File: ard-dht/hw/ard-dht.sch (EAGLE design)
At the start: 7 parts, among them U1 ATMEGA328P_PDIP

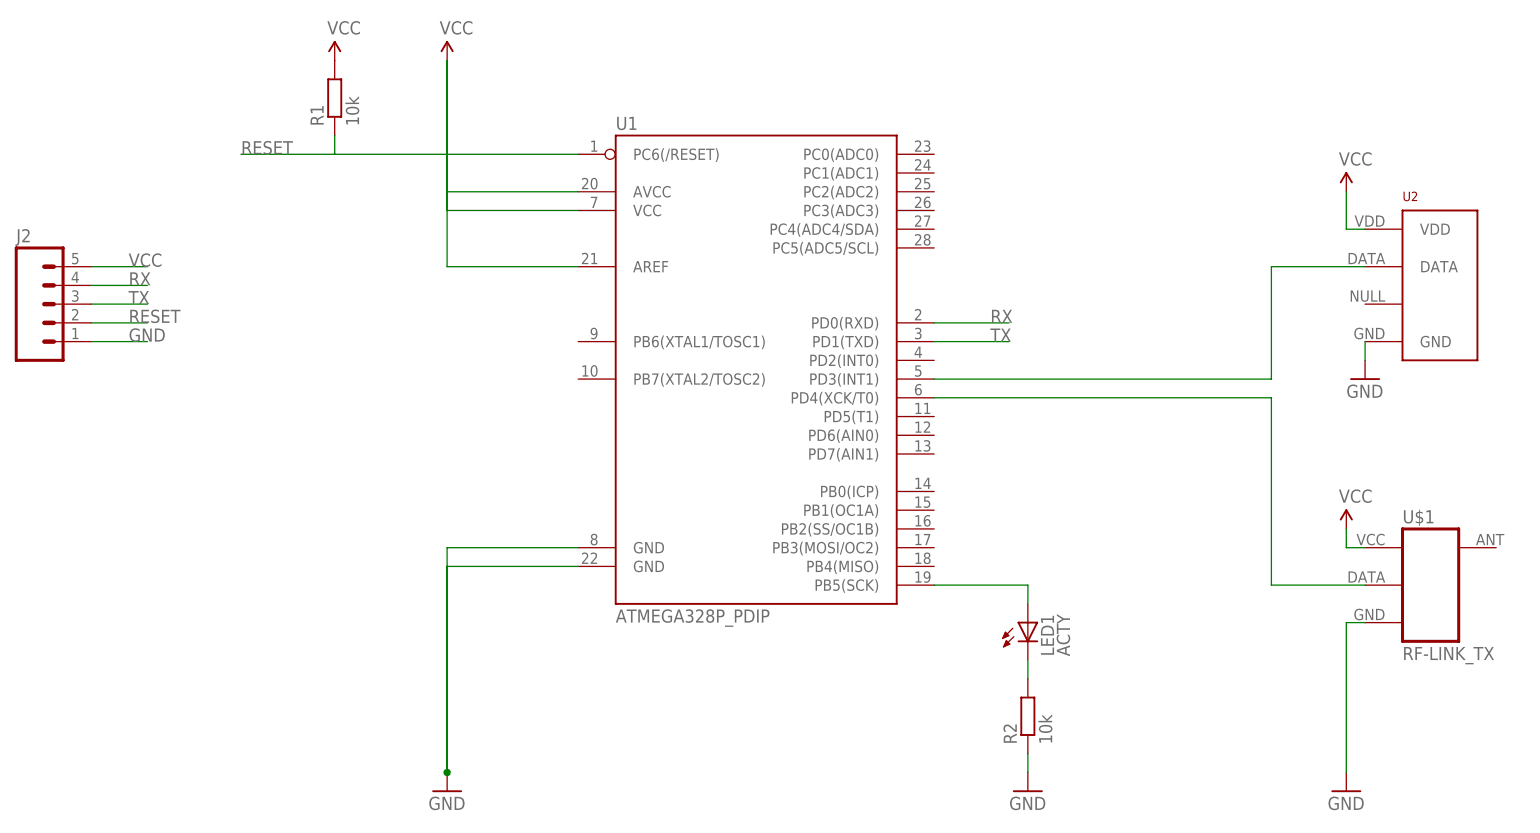
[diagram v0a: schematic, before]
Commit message: Using I/O pins to provide power to : 	- Temperature sensor (DHT) 	- RF emitter The Atmega328p is now used fully in power down mode. Wake up is performed regularly by using an external RC pair. Moved also the led output pin, the ease routing.
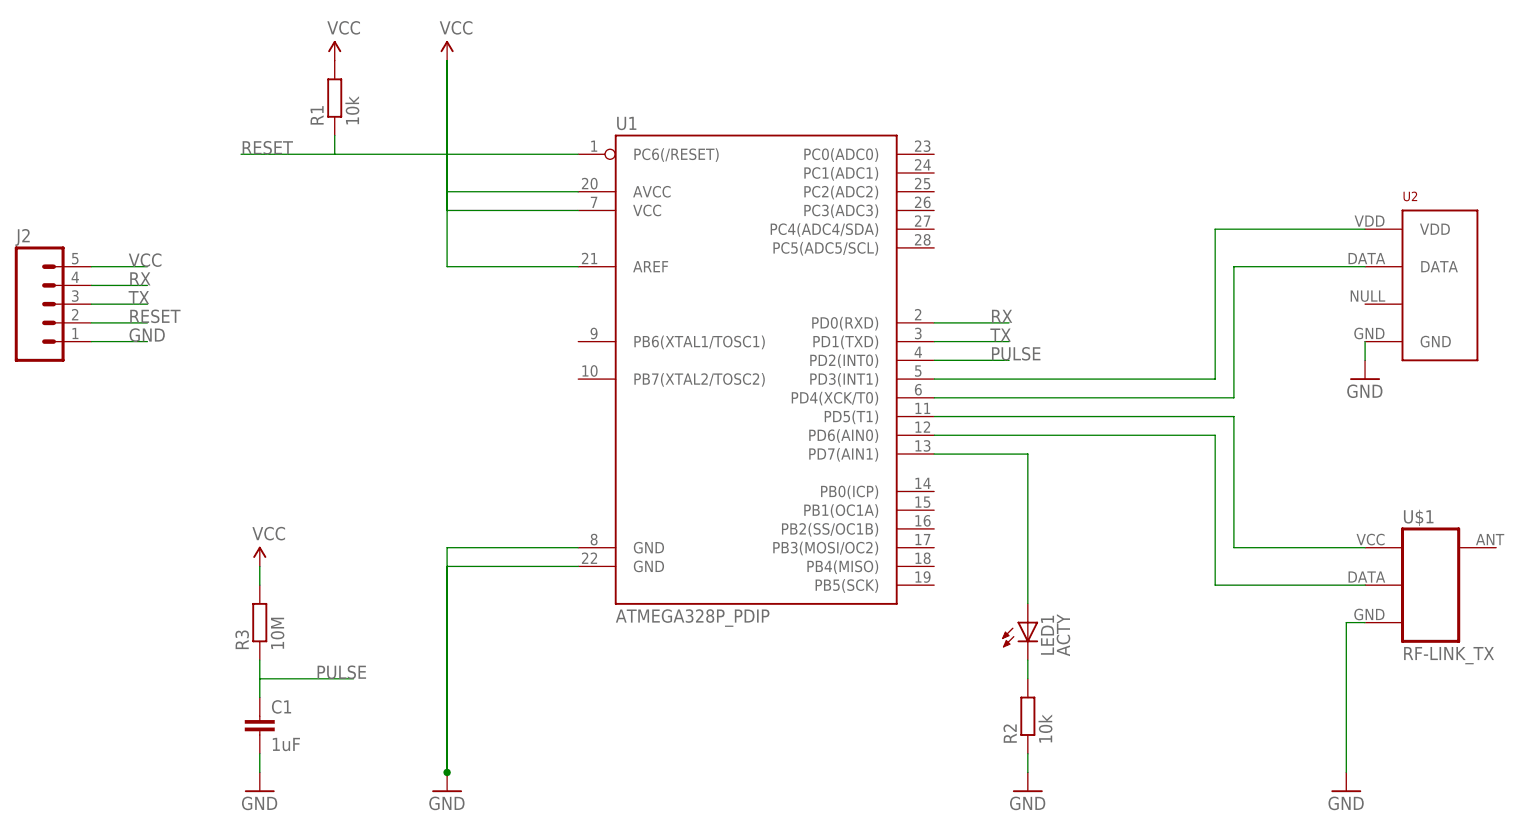
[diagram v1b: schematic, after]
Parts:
- added C1: 1uF, capacitor-wima:C5/5
- added R3: 10M, eagle-ltspice:R0204/7
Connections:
- new net N$5: U1.PD4(XCK/T0), U2.DATA
- new net N$6: U$1.DATA, U1.PD6(AIN0)
- new net PULSE: C1.1, R3.1, U1.PD2(INT0)
- net GND: now also C1.2
- net N$1: now also U2.VDD; no longer U2.DATA
- net N$2: now also U$1.+5V, U1.PD5(T1); no longer U$1.DATA, U1.PD4(XCK/T0)
- net N$3: now also U1.PD7(AIN1); no longer U1.PB5(SCK)
- net VCC: now also R3.2; no longer U$1.+5V, U2.VDD
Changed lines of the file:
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@@
 <part name="R1" library="resistor" deviceset="R-EU_" device="0207/10" value="10k"/>
 <part name="U2" library="RHT03_DHT-22_AM2302" deviceset="RHT03_DHT-22_AM2302" device=""/>
-<part name="SUPPLY3" library="SparkFun-Aesthetics" deviceset="VCC" device=""/>
 <part name="GND2" library="SparkFun-Aesthetics" deviceset="GND" device=""/>
 <part name="U$1" library="SparkFun-RF" deviceset="RF-LINK_TX" device=""/>
-<part name="SUPPLY4" library="SparkFun-Aesthetics" deviceset="VCC" device=""/>
 <part name="GND4" library="SparkFun-Aesthetics" deviceset="GND" device=""/>
 <part name="GND6" library="SparkFun-Aesthetics" deviceset="GND" device=""/>
@@
 <part name="LED1" library="led" deviceset="LED" device="3MM" value="ACTY"/>
 <part name="R2" library="eagle-ltspice" deviceset="R" device="0204/7" value="10k"/>
+<part name="GND3" library="SparkFun-Aesthetics" deviceset="GND" device=""/>
+<part name="SUPPLY3" library="SparkFun-Aesthetics" deviceset="VCC" device=""/>
+<part name="C1" library="capacitor-wima" deviceset="C" device="5/5" value="1uF"/>
+<part name="R3" library="eagle-ltspice" deviceset="R" device="0204/7" value="10M"/>
 </parts>
 <sheets>
@@
 <instance part="R1" gate="G$1" x="17.78" y="86.36" rot="R90"/>
 <instance part="U2" gate="G$1" x="167.64" y="60.96"/>
-<instance part="SUPPLY3" gate="G$1" x="154.94" y="73.66"/>
 <instance part="GND2" gate="1" x="157.48" y="48.26"/>
 <instance part="U$1" gate="G$1" x="165.1" y="22.86"/>
-<instance part="SUPPLY4" gate="G$1" x="154.94" y="27.94"/>
 <instance part="GND4" gate="1" x="154.94" y="-7.62"/>
 <instance part="GND6" gate="1" x="111.76" y="-7.62"/>
@@
 <instance part="LED1" gate="G$1" x="111.76" y="15.24"/>
 <instance part="R2" gate="G$1" x="111.76" y="2.54" rot="R90"/>
+<instance part="GND3" gate="1" x="7.62" y="-7.62"/>
+<instance part="SUPPLY3" gate="G$1" x="7.62" y="22.86"/>
+<instance part="C1" gate="G$1" x="7.62" y="2.54"/>
+<instance part="R3" gate="G$1" x="7.62" y="15.24" rot="R90"/>
 </instances>
 <busses>
@@
 </segment>
 <segment>
-<pinref part="U2" gate="G$1" pin="VDD"/>
-<wire x1="157.48" y1="68.58" x2="154.94" y2="68.58" width="0.1524" layer="91"/>
-<pinref part="SUPPLY3" gate="G$1" pin="VCC"/>
-<wire x1="154.94" y1="68.58" x2="154.94" y2="73.66" width="0.1524" layer="91"/>
-</segment>
-<segment>
-<pinref part="U$1" gate="G$1" pin="+5V"/>
-<wire x1="157.48" y1="25.4" x2="154.94" y2="25.4" width="0.1524" layer="91"/>
-<pinref part="SUPPLY4" gate="G$1" pin="VCC"/>
-<wire x1="154.94" y1="25.4" x2="154.94" y2="27.94" width="0.1524" layer="91"/>
-</segment>
-<segment>
 <pinref part="J2" gate="G$1" pin="5"/>
 <wire x1="-15.24" y1="63.5" x2="-7.62" y2="63.5" width="0.1524" layer="91"/>
 <label x="-10.16" y="63.5" size="1.778" layer="95"/>
+</segment>
+<segment>
+<pinref part="SUPPLY3" gate="G$1" pin="VCC"/>
+<pinref part="R3" gate="G$1" pin="2"/>
+<wire x1="7.62" y1="22.86" x2="7.62" y2="20.32" width="0.1524" layer="91"/>
 </segment>
 </net>
@@
 <wire x1="111.76" y1="-2.54" x2="111.76" y2="-5.08" width="0.1524" layer="91"/>
 </segment>
-</net>
-<net name="N$1" class="0">
-<segment>
-<pinref part="U1" gate="G$1" pin="PD3(INT1)"/>
-<wire x1="99.06" y1="48.26" x2="144.78" y2="48.26" width="0.1524" layer="91"/>
-<pinref part="U2" gate="G$1" pin="DATA"/>
-<wire x1="157.48" y1="63.5" x2="144.78" y2="63.5" width="0.1524" layer="91"/>
-<wire x1="144.78" y1="63.5" x2="144.78" y2="48.26" width="0.1524" layer="91"/>
-</segment>
-</net>
-<net name="N$2" class="0">
-<segment>
-<pinref part="U1" gate="G$1" pin="PD4(XCK/T0)"/>
-<wire x1="99.06" y1="45.72" x2="144.78" y2="45.72" width="0.1524" layer="91"/>
-<wire x1="144.78" y1="45.72" x2="144.78" y2="20.32" width="0.1524" layer="91"/>
-<pinref part="U$1" gate="G$1" pin="DATA"/>
-<wire x1="144.78" y1="20.32" x2="157.48" y2="20.32" width="0.1524" layer="91"/>
+<segment>
+<pinref part="C1" gate="G$1" pin="2"/>
+<pinref part="GND3" gate="1" pin="GND"/>
+<wire x1="7.62" y1="-2.54" x2="7.62" y2="-5.08" width="0.1524" layer="91"/>
 </segment>
 </net>
@@
 </segment>
 </net>
-<net name="N$3" class="0">
-<segment>
-<pinref part="U1" gate="G$1" pin="PB5(SCK)"/>
-<wire x1="99.06" y1="20.32" x2="111.76" y2="20.32" width="0.1524" layer="91"/>
-<pinref part="LED1" gate="G$1" pin="A"/>
-<wire x1="111.76" y1="20.32" x2="111.76" y2="17.78" width="0.1524" layer="91"/>
-</segment>
-</net>
 <net name="N$4" class="0">
 <segment>
@@
 </segment>
 </net>
+<net name="N$3" class="0">
+<segment>
+<pinref part="U1" gate="G$1" pin="PD7(AIN1)"/>
+<wire x1="99.06" y1="38.1" x2="111.76" y2="38.1" width="0.1524" layer="91"/>
+<pinref part="LED1" gate="G$1" pin="A"/>
+<wire x1="111.76" y1="38.1" x2="111.76" y2="17.78" width="0.1524" layer="91"/>
+</segment>
+</net>
+<net name="N$1" class="0">
+<segment>
+<pinref part="U1" gate="G$1" pin="PD3(INT1)"/>
+<wire x1="99.06" y1="48.26" x2="137.16" y2="48.26" width="0.1524" layer="91"/>
+<wire x1="137.16" y1="48.26" x2="137.16" y2="68.58" width="0.1524" layer="91"/>
+<pinref part="U2" gate="G$1" pin="VDD"/>
+<wire x1="137.16" y1="68.58" x2="157.48" y2="68.58" width="0.1524" layer="91"/>
+</segment>
+</net>
+<net name="N$5" class="0">
+<segment>
+<pinref part="U1" gate="G$1" pin="PD4(XCK/T0)"/>
+<wire x1="99.06" y1="45.72" x2="139.7" y2="45.72" width="0.1524" layer="91"/>
+<wire x1="139.7" y1="45.72" x2="139.7" y2="63.5" width="0.1524" layer="91"/>
+<pinref part="U2" gate="G$1" pin="DATA"/>
+<wire x1="139.7" y1="63.5" x2="157.48" y2="63.5" width="0.1524" layer="91"/>
+</segment>
+</net>
+<net name="N$2" class="0">
+<segment>
+<pinref part="U1" gate="G$1" pin="PD5(T1)"/>
+<wire x1="99.06" y1="43.18" x2="139.7" y2="43.18" width="0.1524" layer="91"/>
+<wire x1="139.7" y1="43.18" x2="139.7" y2="25.4" width="0.1524" layer="91"/>
+<pinref part="U$1" gate="G$1" pin="+5V"/>
+<wire x1="139.7" y1="25.4" x2="157.48" y2="25.4" width="0.1524" layer="91"/>
+</segment>
+</net>
+<net name="N$6" class="0">
+<segment>
+<pinref part="U1" gate="G$1" pin="PD6(AIN0)"/>
+<wire x1="99.06" y1="40.64" x2="137.16" y2="40.64" width="0.1524" layer="91"/>
+<wire x1="137.16" y1="40.64" x2="137.16" y2="20.32" width="0.1524" layer="91"/>
+<pinref part="U$1" gate="G$1" pin="DATA"/>
+<wire x1="137.16" y1="20.32" x2="157.48" y2="20.32" width="0.1524" layer="91"/>
+</segment>
+</net>
+<net name="PULSE" class="0">
+<segment>
+<pinref part="U1" gate="G$1" pin="PD2(INT0)"/>
+<wire x1="99.06" y1="50.8" x2="109.22" y2="50.8" width="0.1524" layer="91"/>
+<label x="106.68" y="50.8" size="1.778" layer="95"/>
+</segment>
+<segment>
+<pinref part="R3" gate="G$1" pin="1"/>
+<pinref part="C1" gate="G$1" pin="1"/>
+<wire x1="7.62" y1="10.16" x2="7.62" y2="7.62" width="0.1524" layer="91"/>
+<wire x1="7.62" y1="7.62" x2="7.62" y2="5.08" width="0.1524" layer="91"/>
+<wire x1="7.62" y1="7.62" x2="20.32" y2="7.62" width="0.1524" layer="91"/>
+<label x="15.24" y="7.62" size="1.778" layer="95"/>
+</segment>
+</net>
